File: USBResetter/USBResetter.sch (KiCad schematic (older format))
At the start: 13 parts, among them J1 USB In, J2 USB On, J3 USB Out, Q1 BC547, SW1 Bypass, U1 ASSR-1218

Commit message: Rev A (#1)
* Update README.md

* Update README.md

* Layout Formatting

General layout tidy up.

* PCB Layout, Parts Assignment

* Fixed issues with components and layout

Replaced Footprint for NPN Transistor to match the Pinout of the Part. Recreated the Data lines using Differential Pair to ensure optimal USB Data speed and minimal interference.
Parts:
- D1, D2: footprint (none) -> LEDs:LED_1206
- J1, J3: footprint (none) -> Connectors:USB_A
- J2: footprint (none) -> Pin_Headers:Pin_Header_Straight_1x02_Pitch2.54mm
- Q1: footprint (none) -> TO_SOT_Packages_SMD:SOT-23; symbol Device:Q_NPN_BCE -> Device:Q_NPN_BEC
- R1, R2, R3, R4, R5: footprint (none) -> Resistors_SMD:R_0805
- SW1: footprint (none) -> Buttons_Switches_SMD:SW_SPST_EVPBF
- U1: footprint Package_SO:SO-4_4.4x4.3mm_P2.54mm -> Housings_SOIC:SO-4_4.4x4.3mm_Pitch2.54mm
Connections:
- net Bypass: now also Q1.3 (C); no longer Q1.2 (C)
- net GND: now also Q1.2 (E); no longer Q1.3 (E)
- net USBD-: now reaches J1.2 (D-), J3.2 (D-)
- net USBD+: now reaches J1.3 (D+), J3.3 (D+)
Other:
- note added: "Indicators"
- note added: "Main Isolator"
- note added: "Manual Bypass"
- moved on the sheet: D1, D2, J1, J2, J3, Q1, R1, R2, R3, R4, R5, SW1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

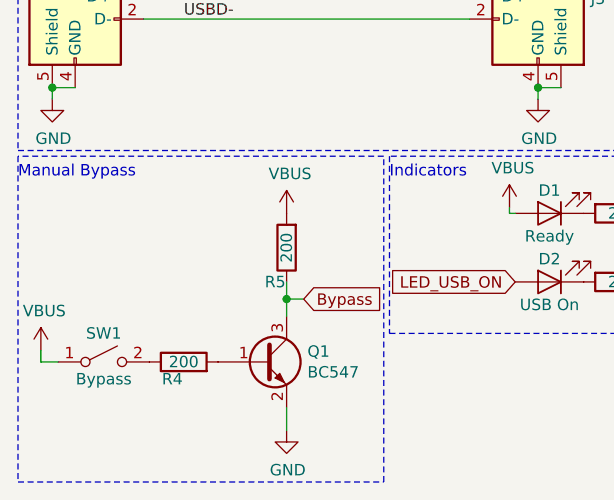
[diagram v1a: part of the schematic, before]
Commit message: Fixed Bypass Transistor issue
Removed current limiting resistor and connection to ground for the Bypass Transistor, to allow it to work as intended.
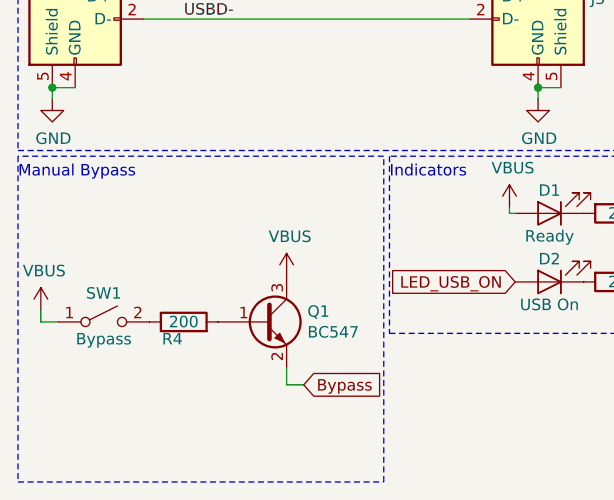
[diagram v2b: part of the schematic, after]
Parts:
- removed R5: 200, Resistors_SMD:R_0805, symbol Device:R
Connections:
- net Bypass: now also Q1.2 (E); no longer Q1.3 (C)
- net GND: no longer Q1.2 (E)
- net VBUS: now also Q1.3 (C)
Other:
- moved on the sheet: Q1, R4, SW1
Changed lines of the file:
@@
 EESchema Schematic File Version 4
+LIBS:USBResetter-cache
 EELAYER 29 0
 EELAYER END
@@
 	2300 1500 2550 1500
 $Comp
-L Device:Q_NPN_BEC Q1
-U 1 1 5D050F17
-P 1650 3300
-F 0 "Q1" H 1841 3346 50  0000 L CNN
-F 1 "BC547" H 1841 3255 50  0000 L CNN
-F 2 "TO_SOT_Packages_SMD:SOT-23" H 1850 3400 50  0001 C CNN
-F 3 "~" H 1650 3300 50  0001 C CNN
-	1    1650 3300
-	1    0    0    -1
-$EndComp
-$Comp
 L power:VBUS #PWR0105
 U 1 1 5D056FC9
@@
 	2725 2650 2750 2650
 $Comp
-L power:VBUS #PWR0107
-U 1 1 5D059CF8
-P 675 3250
-F 0 "#PWR0107" H 675 3100 50  0001 C CNN
-F 1 "VBUS" H 690 3423 50  0000 C CNN
-F 2 "" H 675 3250 50  0001 C CNN
-F 3 "" H 675 3250 50  0001 C CNN
-	1    675  3250
-	1    0    0    -1
-$EndComp
-Wire Wire Line
-	675  3250 675  3300
-Wire Wire Line
-	675  3300 750  3300
-$Comp
-L Switch:SW_SPST SW1
-U 1 1 5D05B778
-P 950 3300
-F 0 "SW1" H 950 3425 50  0000 C CNN
-F 1 "Bypass" H 950 3225 50  0000 C CNN
-F 2 "Buttons_Switches_SMD:SW_SPST_EVPBF" H 950 3300 50  0001 C CNN
-F 3 "~" H 950 3300 50  0001 C CNN
-	1    950  3300
-	1    0    0    -1
-$EndComp
-$Comp
 L power:VBUS #PWR0108
 U 1 1 5D05C5BA
-P 1750 2650
-F 0 "#PWR0108" H 1750 2500 50  0001 C CNN
-F 1 "VBUS" H 1765 2823 50  0000 C CNN
-F 2 "" H 1750 2650 50  0001 C CNN
-F 3 "" H 1750 2650 50  0001 C CNN
-	1    1750 2650
+P 1750 2925
+F 0 "#PWR0108" H 1750 2775 50  0001 C CNN
+F 1 "VBUS" H 1765 3098 50  0000 C CNN
+F 2 "" H 1750 2925 50  0001 C CNN
+F 3 "" H 1750 2925 50  0001 C CNN
+	1    1750 2925
 	1    0    0    -1
 $EndComp
@@
 Wire Wire Line
 	2100 1500 2300 1500
-Text GLabel 1825 3025 2    50   Input ~ 0
+Text GLabel 1825 3400 2    50   Input ~ 0
 Bypass
-$Comp
-L power:GND #PWR0109
-U 1 1 5D060911
-P 1750 3600
-F 0 "#PWR0109" H 1750 3350 50  0001 C CNN
-F 1 "GND" H 1755 3427 50  0000 C CNN
-F 2 "" H 1750 3600 50  0001 C CNN
-F 3 "" H 1750 3600 50  0001 C CNN
-	1    1750 3600
-	1    0    0    -1
-$EndComp
-$Comp
-L Device:R R5
-U 1 1 5D0617B8
-P 1750 2800
-F 0 "R5" H 1800 2950 50  0000 C CNN
-F 1 "200" V 1750 2800 50  0000 C CNN
-F 2 "Resistors_SMD:R_0805" V 1680 2800 50  0001 C CNN
-F 3 "~" H 1750 2800 50  0001 C CNN
-	1    1750 2800
-	-1   0    0    1
-$EndComp
-Wire Wire Line
-	1750 2950 1750 3025
-Wire Wire Line
-	1825 3025 1750 3025
-Connection ~ 1750 3025
-Wire Wire Line
-	1750 3025 1750 3100
-Wire Wire Line
-	1750 3500 1750 3600
-$Comp
-L Device:R R4
-U 1 1 5D065D8A
-P 1300 3300
-F 0 "R4" V 1225 3350 50  0000 C CNN
-F 1 "200" V 1300 3300 50  0000 C CNN
-F 2 "Resistors_SMD:R_0805" V 1230 3300 50  0001 C CNN
-F 3 "~" H 1300 3300 50  0001 C CNN
-	1    1300 3300
-	0    -1   -1   0
-$EndComp
 Text Notes 1100 675  0    50   ~ 0
 +5V DC
@@
 	2175 2400 575  2400
 Wire Notes Line
-	575  2400 575  3825
-Wire Notes Line
 	3200 2375 3200 575
 Wire Notes Line
 	3200 575  575  575
-Wire Notes Line
-	575  575  575  2375
 Wire Notes Line
 	575  2375 3200 2375
@@
 Text Label 1300 1800 0    50   ~ 0
 USBD-
+Wire Notes Line
+	575  575  575  2375
+Wire Notes Line
+	575  2400 575  3825
+$Comp
+L Device:R R4
+U 1 1 5D065D8A
+P 1300 3125
+F 0 "R4" V 1225 3175 50  0000 C CNN
+F 1 "200" V 1300 3125 50  0000 C CNN
+F 2 "Resistors_SMD:R_0805" V 1230 3125 50  0001 C CNN
+F 3 "~" H 1300 3125 50  0001 C CNN
+	1    1300 3125
+	0    -1   -1   0
+$EndComp
+$Comp
+L Switch:SW_SPST SW1
+U 1 1 5D05B778
+P 950 3125
+F 0 "SW1" H 950 3250 50  0000 C CNN
+F 1 "Bypass" H 950 3050 50  0000 C CNN
+F 2 "Buttons_Switches_SMD:SW_SPST_EVPBF" H 950 3125 50  0001 C CNN
+F 3 "~" H 950 3125 50  0001 C CNN
+	1    950  3125
+	1    0    0    -1
+$EndComp
+Wire Wire Line
+	675  3125 750  3125
+Wire Wire Line
+	675  3075 675  3125
+$Comp
+L power:VBUS #PWR0107
+U 1 1 5D059CF8
+P 675 3075
+F 0 "#PWR0107" H 675 2925 50  0001 C CNN
+F 1 "VBUS" H 690 3248 50  0000 C CNN
+F 2 "" H 675 3075 50  0001 C CNN
+F 3 "" H 675 3075 50  0001 C CNN
+	1    675  3075
+	1    0    0    -1
+$EndComp
+$Comp
+L Device:Q_NPN_BEC Q1
+U 1 1 5D050F17
+P 1650 3125
+F 0 "Q1" H 1841 3171 50  0000 L CNN
+F 1 "BC547" H 1841 3080 50  0000 L CNN
+F 2 "TO_SOT_Packages_SMD:SOT-23" H 1850 3225 50  0001 C CNN
+F 3 "~" H 1650 3125 50  0001 C CNN
+	1    1650 3125
+	1    0    0    -1
+$EndComp
+Wire Wire Line
+	1750 3325 1750 3400
+Wire Wire Line
+	1750 3400 1825 3400
 $EndSCHEMATC

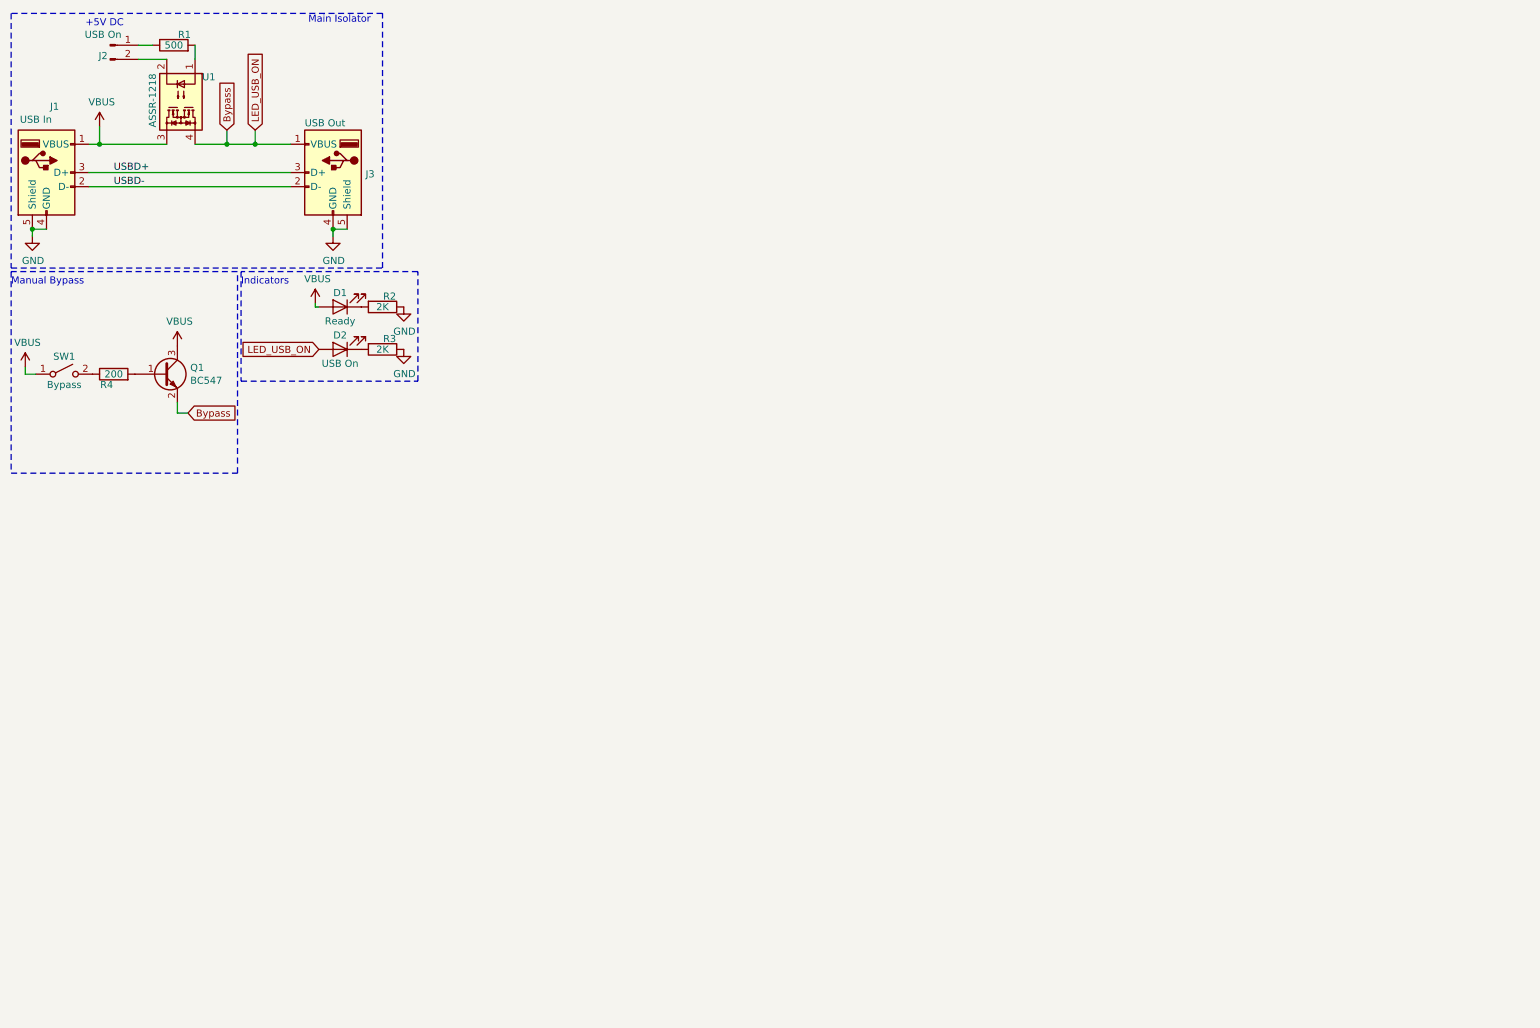
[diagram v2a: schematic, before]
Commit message: Bypass LED, Button Centered
* Added Bypass LED Indicator LED.
* Moved the Bypass button to center of the board.
* Simpliflied the ground plane.
* Properly annotated schematic
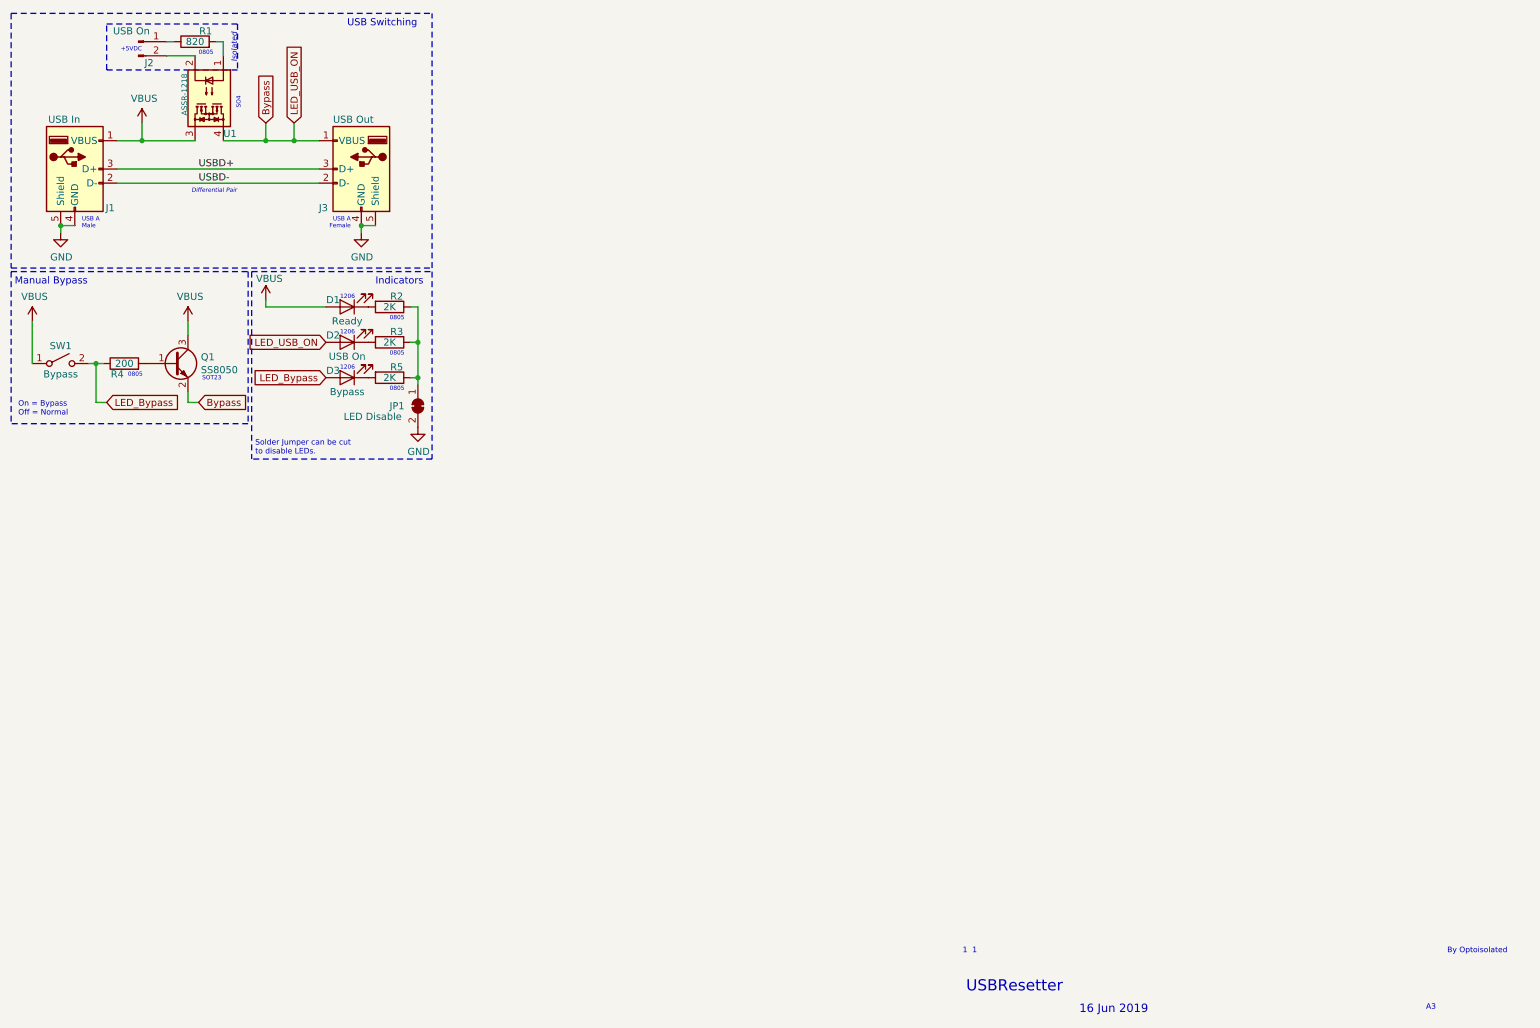
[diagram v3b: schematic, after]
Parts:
- added D3: Bypass, LEDs:LED_1206, symbol Device:LED
- added JP1: LED Disable, Jumpers:SolderJumper-2_P1.3mm_Bridged_Pad1.0x1.5mm, symbol Jumper:SolderJumper_2_Bridged
- added R5: 2K, Resistors_SMD:R_0805, symbol Device:R
- Q1: value BC547 -> SS8050
- R1: value 500 -> 820
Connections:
- net GND: now also JP1.2 (B); no longer R2.1, R3.1
- net LED_Bypass: now reaches R4.1, SW1.2 (B)
- net LED_Bypass: now also D3.2 (A)
- new net: JP1.1 (A), R2.1, R3.1, R5.1
- new net: D3.1 (K), R5.2
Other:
- note added: "+5VDC"
- note added: "0805"
- note added: "1 1"
- note added: "1206"
- note added: "16 Jun 2019"
- note added: "A3"
- note added: "By Optoisolated"
- note added: "Differential Pair"
- note added: "Isolated"
- note added: "On = Bypass\nOff = Normal"
- note added: "SO4"
- note added: "SOT23"
- note added: "Solder Jumper can be cut \nto disable LEDs."
- note added: "USB A\nFemale"
- note added: "USB A\nMale"
- note added: "USB Switching"
- note added: "USBResetter"
- note removed: "+5V DC"
- note removed: "Main Isolator"
- moved on the sheet: D1, D2, J1, J2, J3, Q1, R1, R2, R3, R4, SW1, U1
